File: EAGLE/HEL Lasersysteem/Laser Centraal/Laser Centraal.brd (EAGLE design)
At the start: 90 x 35 mm, 82 parts, among them IC1 LMV324M, IC2 LMV324M, IC3 74LVC1G14DBV, IC6 ATMEGA328P-AU, IC7 FT232RL

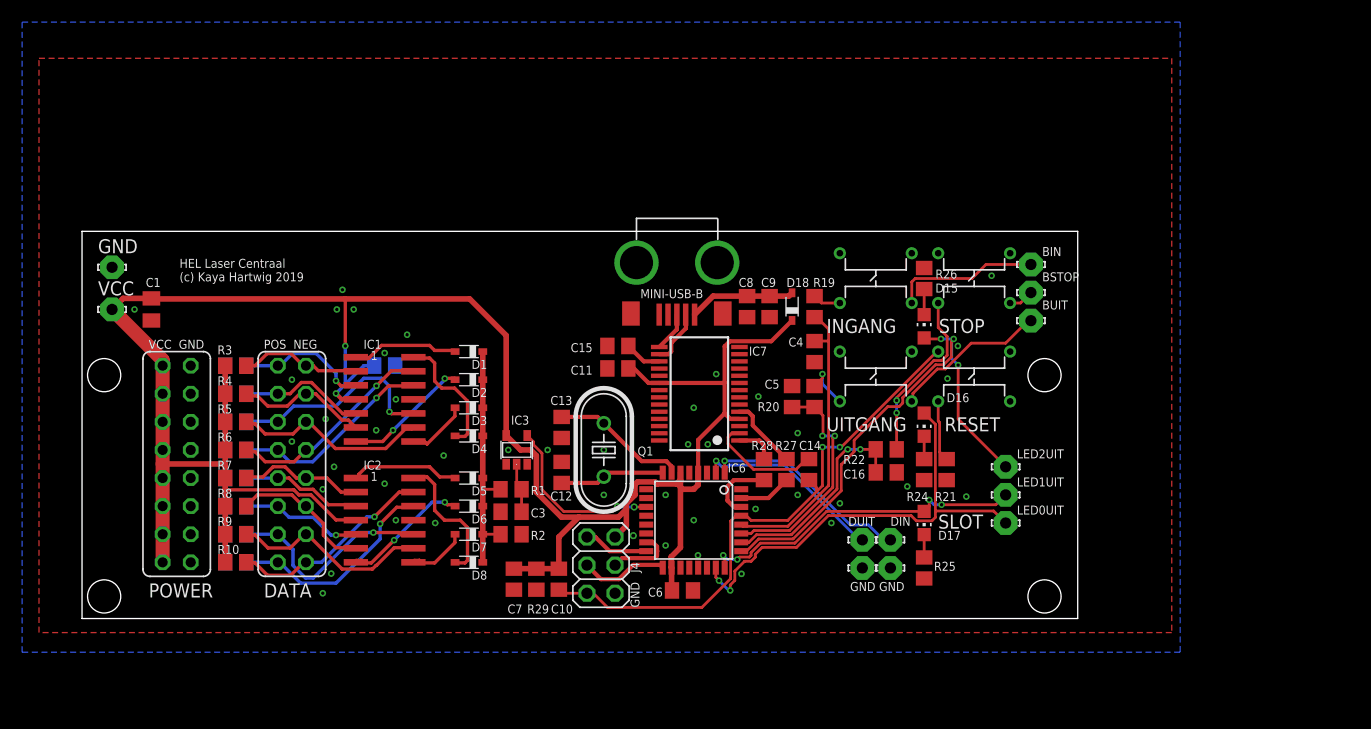
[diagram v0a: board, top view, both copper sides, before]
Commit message: Laser PCB's aangepast
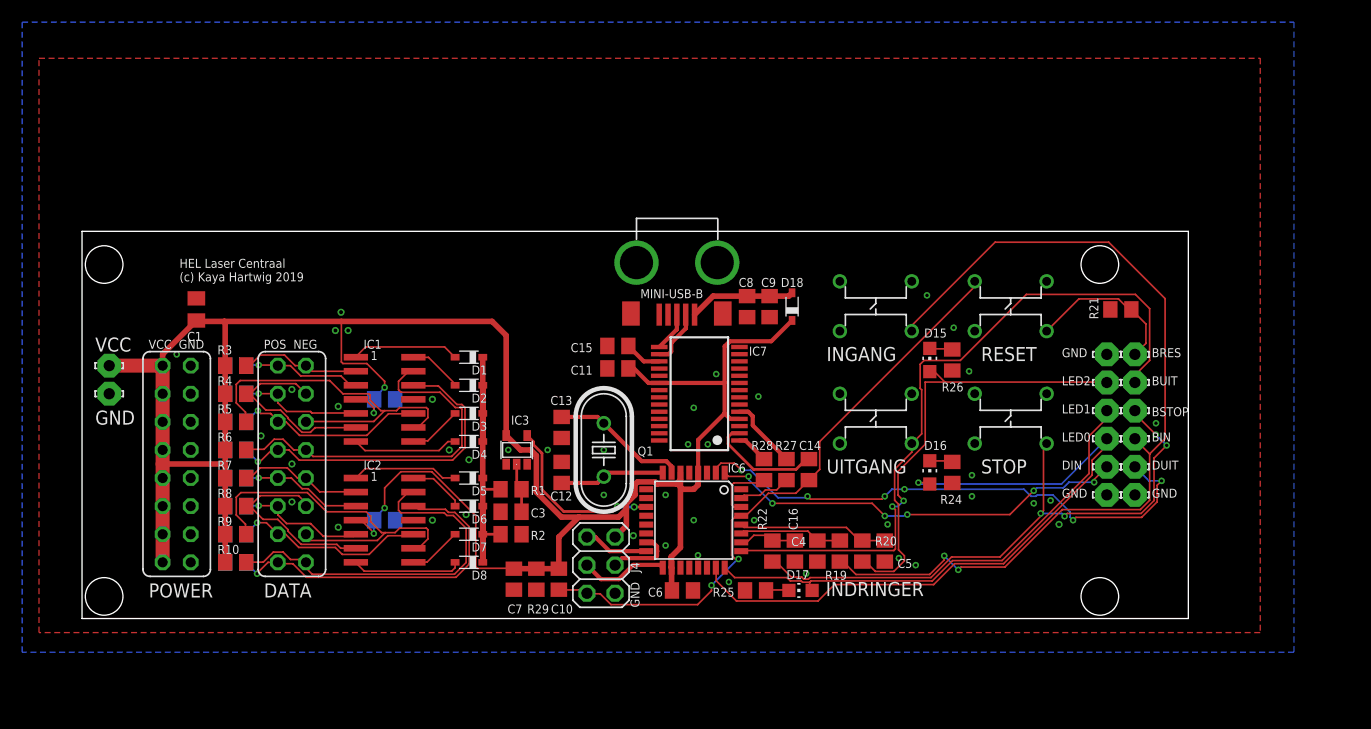
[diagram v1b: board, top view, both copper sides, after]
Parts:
- removed LED0UIT, LED1UIT, LED2UIT: LSP10, solpad:LSP10
- added BRES, LED0, LED1, LED2, OUTGND2: LSP10, solpad:LSP10
- added C17: 100n, rcl:C0805
- moved DUIT 25.5 mm to (90.2, 13.7), turned to 180 degrees
- moved OUTGND 23.1 mm to (87.6, 11.2)
- moved OUTGND1 23.1 mm to (90.2, 11.2)
- moved R19 22.2 mm to (63.5, 6.10), turned to 90 degrees
- moved R21 21.4 mm to (88.9, 27.9), turned to 180 degrees
- moved DIN 20.6 mm to (87.6, 13.7)
- moved BIN 18.3 mm to (90.2, 16.3)
- moved C4 18.0 mm to (61.5, 6.10)
- moved C5 16.3 mm to (67.6, 6.10), turned to 270 degrees
- moved R25 15.4 mm to (55.9, 2.54), turned to 180 degrees
- moved R20 14.6 mm to (65.5, 6.10), turned to 90 degrees
- moved BSTOP 14.2 mm to (90.2, 18.8)
- moved R22 13.8 mm to (57.4, 6.10), turned to 90 degrees
- moved STOP 13.1 mm to (75.7, 20.3)
- moved D17 12.7 mm to (59.9, 2.54), turned to 90 degrees
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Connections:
- net BUTTIN: now also IC6.27; no longer IC6.28
- net BUTTOUT: now also IC6.28; no longer IC6.27
- net GND: now also C17.2, OUTGND2.MP
- net N$13: now also LED1.MP; no longer LED1UIT.MP
- net N$15: now also BRES.MP
- net N$16: now also LED0.MP; no longer LED0UIT.MP
- net N$2: now also D4.A; no longer D2.A
- net N$22: now also LED2.MP; no longer LED2UIT.MP
- net N$4: now also D2.A; no longer D4.A
- net N$6: now also D8.A; no longer D6.A
- net N$8: now also D6.A; no longer D8.A
- net VCC: now also C17.1
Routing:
- net BUTTINX: track 15.9 -> 81.9 mm, vias 0 -> 2
- net BUTTSTOPX: track 18.2 -> 54.8 mm, vias 2 -> 4
- net BUTTOUTX: track 18.7 -> 54.9 mm, vias 1 -> 0
- net N$20: track 17.4 -> 49.5 mm, vias 1 -> 6
- net N$16: track 41.9 -> 64.3 mm, vias 2 -> 1
- net N$23: track 19.0 -> 38.3 mm, vias 1 -> 6
- net BUTTIN: track 26.6 -> 9.36 mm
- net LAS-7: track 18.7 -> 34.2 mm, vias 1 -> 0
- net LAS-2: track 17.9 -> 32.8 mm
- net N$9: track 22.3 -> 37.0 mm
- net N$13: track 30.1 -> 44.8 mm, vias 4 -> 0
- net LAS-6: track 19.1 -> 33.5 mm
- net LAS-3: track 19.0 -> 33.2 mm, vias 1 -> 0
- net BUTTSTOP: track 19.3 -> 5.31 mm, vias 2 -> 0
- net LAS+3: track 18.4 -> 30.6 mm
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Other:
- board size 90 x 35 mm -> 100 x 35 mm
- board text added: "INDRINGER"
- board text removed: "GND GND"
- board text removed: "SLOT"

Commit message: tweede versie laser gerbers klaargemaakt voor bestelling
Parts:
- removed C14, C15, C9: 100nF, rcl:C0805
- removed D18: BAT60J, diode:SOD323_ST
- removed IC7: FT232RL, ftdichip:SSOP28
- removed MINI-USB-B: MINI_USB_B-KRHRO-SELECU-M-M5DS-W-4, mini USB B Korean Hroparts Elec U-M-M5DS-W-4:KRHROSELECU-M-M5DS-W-4
- removed R27, R28: 1k, rcl:R0805
- added R23: 100, rcl:R0805
- added RX, TX: LSP10, solpad:LSP10
- C1: device rcl:C0805K -> rcl:C0805
- C8: value 4u7 -> 100n
- moved C8 46.6 mm to (8.50, 26.5), turned to 0 degrees
- moved C7 28.8 mm to (56.3, 21.9), turned to 0 degrees
- moved C10 19.3 mm to (55.3, 5.50), turned to 0 degrees
- moved R29 17.2 mm to (55.3, 3.40), turned to 0 degrees
- moved C12 15.3 mm to (52.2, 19.8), turned to 180 degrees
- moved C13 14.6 mm to (52.2, 21.9), turned to 180 degrees
- moved C11 13.2 mm to (56.3, 19.8), turned to 0 degrees
- moved R25 10.3 mm to (66.2, 3.30), turned to 270 degrees
- moved R22 8.89 mm to (66.2, 7.40)
- moved D17 8.39 mm to (68.3, 3.30), turned to 0 degrees
- moved C6 7.87 mm to (55.3, 7.60)
- moved Q1 7.58 mm to (47.2, 20.9)
- moved INGANG 7.50 mm to (71.0, 30.5)
- moved UITGANG 7.50 mm to (71.0, 20.3)
- moved R24 7.47 mm to (66.2, 13.5)
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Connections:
- removed net 3V3: C15.1, IC7.17
- removed net N$19: IC7.15, MINI-USB-B.D+
- removed net N$24: IC7.16, MINI-USB-B.D-
- removed net RX: IC7.1, R28.2
- removed net TX: IC7.5, R27.2
- removed net VUSB: C8.1, C9.1, D18.A, MINI-USB-B.VBUS
- net D0/RX: now also RX.MP; no longer R28.1
- net D1/TX: now also TX.MP; no longer R27.1
- net GND: no longer C15.2, C9.2, IC7.18, IC7.21, IC7.25, IC7.26, IC7.7, MINI-USB-B.GND1, MINI-USB-B.GND2, MINI-USB-B.GND3, MINI-USB-B.GND4, MINI-USB-B.GND5
- net N$15: no longer BRES.MP
- net N$18: now also BRES.MP, R23.2; no longer C14.2, IC7.2
- net RESET: now also R23.1; no longer C14.1
- net VCC: now also C8.1; no longer D18.C, IC7.20, IC7.4
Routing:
- net GND: track 0.00 -> 63.7 mm, vias 44 -> 40
- net RESET: track 55.4 -> 101.5 mm, vias 2 -> 0
- net N$13: track 44.8 -> 90.8 mm, vias 0 -> 2
- net VCC: track 212.1 -> 186.8 mm
- net BUTTINX: track 81.9 -> 57.9 mm, vias 2 -> 4
- net N$20: track 49.5 -> 73.3 mm, vias 6 -> 4
- net BUTTOUTX: track 54.9 -> 78.3 mm, vias 0 -> 6
- net N$16: track 64.3 -> 43.0 mm, vias 1 -> 4
- net VUSB: track 9.63 -> 0.00 mm
- net N$15: track 14.3 -> 6.38 mm
- net N$18: track 10.4 -> 2.57 mm
- net TX: track 6.51 -> 0.00 mm
- net BUTTSTOPX: track 54.8 -> 49.5 mm, vias 4 -> 6
- net N$24: track 5.08 -> 0.00 mm
- net BUTTIN: track 9.36 -> 13.3 mm
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
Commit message: vergeten bestandjes toegevoegd
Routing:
- net VCC: track 186.8 -> 211.8 mm
- net GND: vias 40 -> 47
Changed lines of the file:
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@@
 <drawing>
 <settings>
-<setting alwaysvectorfont="yes"/>
+<setting alwaysvectorfont="no"/>
 <setting verticaltext="up"/>
 </settings>
@@
 <wire x1="53.8" y1="8.15" x2="54.35" y2="7.6" width="0.1524" layer="1"/>
 <wire x1="2.46" y1="22.86" x2="7.29" y2="22.86" width="1.27" layer="1"/>
-<wire x1="7.29" y1="22.86" x2="7.29" y2="20.32635" width="1.27" layer="1"/>
+<wire x1="7.29" y1="22.86" x2="7.29" y2="21.6" width="1.27" layer="1"/>
 <contactref element="C8" pad="1"/>
+<wire x1="7.29" y1="21.6" x2="7.29" y2="20.32635" width="1.27" layer="1"/>
 <wire x1="7.29" y1="20.32635" x2="7.29" y2="20.32" width="1.27" layer="1"/>
 <wire x1="7.29" y1="20.32" x2="7.29" y2="17.81175" width="1.27" layer="1"/>
@@
 <wire x1="7.29" y1="17.78" x2="7.29" y2="15.24" width="1.27" layer="1"/>
 <wire x1="7.29" y1="15.24" x2="7.29" y2="15.2273" width="1.27" layer="1"/>
-<wire x1="7.29" y1="15.2273" x2="7.29" y2="13.97" width="1.27" layer="1"/>
-<wire x1="7.29" y1="13.97" x2="7.29" y2="12.7127" width="1.27" layer="1"/>
+<wire x1="7.29" y1="15.2273" x2="7.29" y2="12.7127" width="1.27" layer="1"/>
 <wire x1="7.29" y1="12.7127" x2="7.29" y2="12.7" width="1.27" layer="1"/>
 <wire x1="7.29" y1="12.7" x2="7.29" y2="10.1981" width="1.27" layer="1"/>
@@
 <wire x1="12.92225" y1="20.2565" x2="12.94" y2="20.32" width="0.1524" layer="1"/>
 <wire x1="12.92225" y1="17.81175" x2="12.94" y2="17.78" width="0.1524" layer="1"/>
-<wire x1="12.92225" y1="20.3962" x2="12.92225" y2="22.84095" width="0.1524" layer="1"/>
+<wire x1="12.92225" y1="20.3962" x2="12.92225" y2="21.6" width="0.1524" layer="1"/>
+<wire x1="12.92225" y1="21.6" x2="12.92225" y2="22.84095" width="0.1524" layer="1"/>
 <wire x1="12.92225" y1="22.84095" x2="12.94" y2="22.86" width="0.1524" layer="1"/>
 <wire x1="12.92225" y1="20.3962" x2="12.94" y2="20.32" width="0.1524" layer="1"/>
 <wire x1="26.4033" y1="20.04695" x2="26.4033" y2="19.8374" width="0.1524" layer="16"/>
 <wire x1="27.31135" y1="20.955" x2="26.4033" y2="20.04695" width="0.1524" layer="16"/>
-<wire x1="27.31135" y1="21.5138" x2="27.31135" y2="20.955" width="0.1524" layer="1"/>
-<wire x1="25.77465" y1="23.0505" x2="27.31135" y2="21.5138" width="0.1524" layer="1"/>
-<wire x1="21.3741" y1="23.0505" x2="25.77465" y2="23.0505" width="0.1524" layer="1"/>
-<wire x1="20.32635" y1="24.09825" x2="21.3741" y2="23.0505" width="0.1524" layer="1"/>
+<wire x1="21.3741" y1="23.0505" x2="20.32635" y2="24.09825" width="0.1524" layer="1"/>
 <wire x1="14.17955" y1="24.09825" x2="20.32635" y2="24.09825" width="0.1524" layer="1"/>
 <wire x1="12.9921" y1="22.9108" x2="14.17955" y2="24.09825" width="0.1524" layer="1"/>
 <wire x1="26.4033" y1="19.8374" x2="26.4" y2="19.81" width="0.1524" layer="16"/>
 <wire x1="12.9921" y1="22.9108" x2="12.94" y2="22.86" width="0.1524" layer="1"/>
-<wire x1="12.92225" y1="15.2273" x2="12.92225" y2="13.97" width="0.1524" layer="1"/>
-<wire x1="12.92225" y1="13.97" x2="12.92225" y2="12.7127" width="0.1524" layer="1"/>
+<wire x1="12.92225" y1="15.2273" x2="12.92225" y2="12.7127" width="0.1524" layer="1"/>
 <wire x1="12.92225" y1="12.7127" x2="12.94" y2="12.7" width="0.1524" layer="1"/>
 <wire x1="12.92225" y1="15.2273" x2="12.94" y2="15.24" width="0.1524" layer="1"/>
-<wire x1="12.92225" y1="13.97" x2="7.29" y2="13.97" width="0.1524" layer="1"/>
 <wire x1="26.33345" y1="7.6835" x2="26.33345" y2="8.87095" width="0.1524" layer="16"/>
-<wire x1="26.05405" y1="7.9629" x2="26.33345" y2="7.6835" width="0.1524" layer="1"/>
-<wire x1="26.05405" y1="8.03275" x2="26.05405" y2="7.9629" width="0.1524" layer="1"/>
-<wire x1="25.21585" y1="8.87095" x2="26.05405" y2="8.03275" width="0.1524" layer="1"/>
+<wire x1="26.33345" y1="7.75335" x2="26.33345" y2="7.6835" width="0.1524" layer="1"/>
+<wire x1="26.33345" y1="7.75335" x2="25.21585" y2="8.87095" width="0.1524" layer="1"/>
 <wire x1="24.79675" y1="8.87095" x2="25.21585" y2="8.87095" width="0.1524" layer="1"/>
 <wire x1="26.33345" y1="8.87095" x2="26.4" y2="8.89" width="0.1524" layer="16"/>
@@
 <wire x1="54.55285" y1="17.95145" x2="54.6" y2="17.9926" width="0.1524" layer="1"/>
 <wire x1="39.116" y1="16.55445" x2="39.116" y2="16.4846" width="0.1524" layer="1"/>
-<wire x1="28.7782" y1="22.9108" x2="27.3812" y2="21.5138" width="0.1524" layer="1"/>
-<wire x1="31.08325" y1="22.9108" x2="28.7782" y2="22.9108" width="0.1524" layer="1"/>
-<wire x1="33.1089" y1="20.88515" x2="31.08325" y2="22.9108" width="0.1524" layer="1"/>
-<wire x1="33.1089" y1="20.6756" x2="33.1089" y2="20.88515" width="0.1524" layer="1"/>
+<wire x1="33.1089" y1="20.88515" x2="33.1089" y2="20.6756" width="0.1524" layer="1"/>
 <wire x1="34.15665" y1="19.62785" x2="33.1089" y2="20.6756" width="0.1524" layer="1"/>
 <wire x1="34.5059" y1="19.62785" x2="34.15665" y2="19.62785" width="0.1524" layer="1"/>
@@
 <wire x1="34.3662" y1="14.5288" x2="34.925" y2="15.0876" width="0.1524" layer="1"/>
 <wire x1="34.3662" y1="12.22375" x2="34.3662" y2="14.5288" width="0.1524" layer="1"/>
-<wire x1="27.3812" y1="21.5138" x2="27.31135" y2="21.5138" width="0.1524" layer="1"/>
 <via x="26.33345" y="18.5801" extent="1-16" drill="0.3"/>
 <via x="27.31135" y="20.955" extent="1-16" drill="0.3"/>
@@
 <wire x1="55.35" y1="19.8" x2="56.2" y2="18.95" width="0.1524" layer="1"/>
 <wire x1="56.2" y1="18.95" x2="56.2" y2="17.9926" width="0.1524" layer="1"/>
-<wire x1="27.31135" y1="21.5138" x2="27.31135" y2="22.6687375" width="0.1524" layer="1"/>
-<wire x1="27.31135" y1="22.6687375" x2="28.765821875" y2="24.123209375" width="0.1524" layer="1"/>
-<wire x1="28.765821875" y1="24.123209375" x2="31.946790625" y2="24.123209375" width="0.1524" layer="1"/>
-<wire x1="31.946790625" y1="24.123209375" x2="32.953209375" y2="23.116790625" width="0.1524" layer="1"/>
-<wire x1="32.953209375" y1="23.116790625" x2="34.486790625" y2="23.116790625" width="0.1524" layer="1"/>
-<wire x1="34.486790625" y1="23.116790625" x2="35.493209375" y2="24.123209375" width="0.1524" layer="1"/>
-<wire x1="35.493209375" y1="24.123209375" x2="36.704178125" y2="24.123209375" width="0.1524" layer="1"/>
-<wire x1="36.704178125" y1="24.123209375" x2="38.35" y2="22.4773875" width="0.1524" layer="1"/>
-<wire x1="38.35" y1="22.4773875" x2="38.35" y2="16.5" width="0.1524" layer="1"/>
+<wire x1="32.953209375" y1="23.116790625" x2="31.646790625" y2="24.423209375" width="0.1524" layer="1"/>
+<wire x1="32.953209375" y1="23.116790625" x2="34.286790625" y2="23.116790625" width="0.1524" layer="1"/>
+<wire x1="34.286790625" y1="23.116790625" x2="35.593209375" y2="24.423209375" width="0.1524" layer="1"/>
+<wire x1="35.593209375" y1="24.423209375" x2="36.904178125" y2="24.423209375" width="0.1524" layer="1"/>
+<wire x1="36.904178125" y1="24.423209375" x2="38.35" y2="22.9773875" width="0.1524" layer="1"/>
+<wire x1="38.35" y1="22.9773875" x2="38.35" y2="16.5" width="0.1524" layer="1"/>
 <wire x1="34.20416875" y1="12.1968" x2="34.23111875" y2="12.22375" width="0.1524" layer="1"/>
 <wire x1="34.23111875" y1="12.22375" x2="34.3662" y2="12.22375" width="0.1524" layer="1"/>
 <wire x1="31.5722" y1="13.2715" x2="32.6469" y2="12.1968" width="0.1524" layer="1"/>
 <wire x1="32.6469" y1="12.1968" x2="34.20416875" y2="12.1968" width="0.1524" layer="1"/>
+<wire x1="45.66" y1="8.87" x2="36.04355" y2="8.87" width="0.1524" layer="16"/>
+<wire x1="36.04355" y1="8.87" x2="26.33345" y2="18.5801" width="0.1524" layer="16"/>
+<wire x1="27.31135" y1="20.955" x2="27.31135" y2="21.8138" width="0.1524" layer="1"/>
+<wire x1="27.31135" y1="21.8138" x2="26.07465" y2="23.0505" width="0.1524" layer="1"/>
+<wire x1="26.07465" y1="23.0505" x2="21.3741" y2="23.0505" width="0.1524" layer="1"/>
+<wire x1="31.646790625" y1="24.423209375" x2="27.447359375" y2="24.423209375" width="0.1524" layer="1"/>
+<wire x1="27.447359375" y1="24.423209375" x2="26.07465" y2="23.0505" width="0.1524" layer="1"/>
+<wire x1="26.07465" y1="23.0505" x2="30.94355" y2="23.0505" width="0.1524" layer="1"/>
+<wire x1="30.94355" y1="23.0505" x2="33.1089" y2="20.88515" width="0.1524" layer="1"/>
+<wire x1="7.29" y1="21.6" x2="12.92225" y2="21.6" width="0.1524" layer="1"/>
 </signal>
 <signal name="GND">
@@
 <via x="49.8" y="13.7" extent="1-16" drill="0.35"/>
 <via x="35" y="4.1" extent="1-16" drill="0.35"/>
+<via x="27.6" y="23.7" extent="1-16" drill="0.35"/>
+<via x="27.5" y="5.6" extent="1-16" drill="0.35"/>
+<via x="32.2" y="10.8" extent="1-16" drill="0.35"/>
+<via x="32.8" y="13.6" extent="1-16" drill="0.35"/>
+<via x="26.5" y="21.7" extent="1-16" drill="0.35"/>
+<via x="33.6" y="17.3" extent="1-16" drill="0.35"/>
+<via x="27" y="16.3" extent="1-16" drill="0.35"/>
 </signal>
 <signal name="N$1">
 <contactref element="IC1" pad="1"/>
 <contactref element="D1" pad="A"/>
-<wire x1="33.64485" y1="23.67915" x2="33.705871875" y2="23.67915" width="0.1524" layer="1"/>
-<wire x1="32.7749" y1="24.5491" x2="33.64485" y2="23.67915" width="0.1524" layer="1"/>
-<wire x1="25.6375" y1="24.5491" x2="32.7749" y2="24.5491" width="0.1524" layer="1"/>
-<wire x1="24.76555" y1="23.67715" x2="25.6375" y2="24.5491" width="0.1524" layer="1"/>
+<wire x1="32.84485" y1="23.67915" x2="33.705871875" y2="23.67915" width="0.1524" layer="1"/>
+<wire x1="31.7749" y1="24.7491" x2="32.84485" y2="23.67915" width="0.1524" layer="1"/>
+<wire x1="27.3375" y1="24.7491" x2="31.7749" y2="24.7491" width="0.1524" layer="1"/>
+<wire x1="27.3375" y1="24.7491" x2="26.2084" y2="23.62" width="0.1524" layer="1"/>
+<wire x1="24.75" y1="23.62" x2="26.2084" y2="23.62" width="0.1524" layer="1"/>
 <wire x1="33.705871875" y1="23.67915" x2="33.72" y2="23.62" width="0.1524" layer="1"/>
-<wire x1="24.76555" y1="23.67715" x2="24.75" y2="23.62" width="0.1524" layer="1"/>
 </signal>
 <signal name="N$2">
